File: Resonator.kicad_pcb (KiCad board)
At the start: 2 copper layers, 88 parts, among them J1 Conn_02x05_Odd_Even, U1 PCM3060, U2 R-78E5.0-0.5, U3 LD2981ABU33TR, U4 TL074, U5 STM32H750VBTx, U6 R-78E3.3-0.5

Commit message: Chanced regulators and oscillator work.
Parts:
- removed the C11 at (62.7, 30.0)
- removed the C13 at (44.7, 33.4)
- removed the C5 at (44.6, 27.6)
- removed the C7 at (48.4, 30.0)
- removed the L1 at (39.2, 30.9)
- removed the U2 at (53.1, 29.0)
- removed the U3 at (65.0, 34.8)
- added R2: 10k, Resistor_SMD:R_0603_1608Metric, B.Cu at (194.9, 90.2)
- added R3: 470, Resistor_SMD:R_0603_1608Metric, B.Cu at (158.0, 71.9)
- added SW1: SW_Push, Button_Switch_THT:SW_PUSH_6mm, B.Cu at (205.5, 86.5)
- added U4: LD2981ABU50TR, Package_TO_SOT_SMD:SOT-89-3, B.Cu at (184.5, 87.5)
- added Y1: ABM8G-25.000MHZ-18-D2Y-T, Crystal:Crystal_SMD_Abracon_ABM8G-4Pin_3.2x2.5mm, B.Cu at (163.3, 71.4)
- C1: renamed from C33; moved to B.Cu
- C10: renamed from C40; moved to B.Cu
- C11: renamed from C43; footprint Capacitor_SMD:C_0603_1608Metric -> Capacitor_SMD:C_0402_1005Metric; moved to B.Cu
- C12: renamed from C44; footprint Capacitor_SMD:C_0603_1608Metric -> Capacitor_SMD:C_0402_1005Metric; moved to B.Cu
- C13: renamed from C45; footprint Capacitor_SMD:C_0603_1608Metric -> Capacitor_SMD:C_0402_1005Metric; moved to B.Cu
- C14: renamed from C46; moved to B.Cu
- C15: renamed from C47; footprint Capacitor_SMD:C_0603_1608Metric -> Capacitor_SMD:C_0402_1005Metric; moved to B.Cu
- C16: renamed from C1; footprint Capacitor_SMD:C_0603_1608Metric -> Capacitor_SMD:C_0402_1005Metric; moved to B.Cu
- C17: renamed from C2; footprint Capacitor_SMD:C_0603_1608Metric -> Capacitor_SMD:C_0402_1005Metric; moved to B.Cu
- C18: renamed from C3; footprint Capacitor_SMD:C_0603_1608Metric -> Capacitor_SMD:C_0402_1005Metric; moved to B.Cu
- C19: renamed from C4; moved to B.Cu
- C2: renamed from C34; footprint Capacitor_SMD:C_0603_1608Metric -> Capacitor_SMD:C_0402_1005Metric; moved to B.Cu
- C20: renamed from C29; moved to B.Cu
- C21: renamed from C6; moved to B.Cu
- C22: renamed from C30; footprint Capacitor_SMD:C_0603_1608Metric -> Capacitor_SMD:C_0402_1005Metric; moved to B.Cu
- C23: renamed from C8; footprint Capacitor_SMD:C_0603_1608Metric -> Capacitor_SMD:C_0402_1005Metric; moved to B.Cu
- C24: renamed from C9; moved to B.Cu
- C25: renamed from C10; moved to B.Cu
- C26: renamed from C31; footprint Capacitor_SMD:C_0603_1608Metric -> Capacitor_SMD:C_0402_1005Metric; moved to B.Cu
- C27: renamed from C12; footprint Capacitor_SMD:C_0603_1608Metric -> Capacitor_SMD:C_0402_1005Metric; moved to B.Cu
- C28: renamed from C32; moved to B.Cu
- C29: renamed from C14; moved to B.Cu
- C3: renamed from C35; footprint Capacitor_SMD:C_0603_1608Metric -> Capacitor_SMD:C_0402_1005Metric; moved to B.Cu
- C30: renamed from C15; moved to B.Cu
- C31: renamed from C16; moved to B.Cu
- C32: renamed from C17; footprint Capacitor_SMD:C_0603_1608Metric -> Capacitor_SMD:C_0402_1005Metric; moved to B.Cu
- C33: renamed from C18; footprint Capacitor_SMD:C_0603_1608Metric -> Capacitor_SMD:C_0402_1005Metric; moved to B.Cu
- C34: renamed from C19; footprint Capacitor_SMD:C_0603_1608Metric -> Capacitor_SMD:C_0402_1005Metric; moved to B.Cu
- C35: renamed from C20; footprint Capacitor_SMD:C_0603_1608Metric -> Capacitor_SMD:C_0402_1005Metric; moved to B.Cu
- C36: renamed from C21; moved to B.Cu
- C37: renamed from C22; moved to B.Cu
- C38: renamed from C23; moved to B.Cu
- C39: renamed from C24; moved to B.Cu
- C4: renamed from C36; footprint Capacitor_SMD:C_0603_1608Metric -> Capacitor_SMD:C_0402_1005Metric; moved to B.Cu
- C40: renamed from C25; moved to B.Cu
- C41: renamed from C26; moved to B.Cu
- C42: renamed from C27; moved to B.Cu
- C43: renamed from C28; moved to B.Cu
- C5: renamed from C37; footprint Capacitor_SMD:C_0603_1608Metric -> Capacitor_SMD:C_0402_1005Metric; moved to B.Cu
- C6: renamed from C41; value 3p9 -> 22p; footprint Capacitor_SMD:C_0603_1608Metric -> Capacitor_SMD:C_0402_1005Metric; moved to B.Cu
- C7: renamed from C42; value 3p9 -> 22p; footprint Capacitor_SMD:C_0603_1608Metric -> Capacitor_SMD:C_0402_1005Metric; moved to B.Cu
- C8: renamed from C38; moved to B.Cu
- C9: renamed from C39; footprint Capacitor_SMD:C_0603_1608Metric -> Capacitor_SMD:C_0402_1005Metric; moved to B.Cu
- D1, D2, D3, D4, D5, D6, D7, FB1, FB2, J1: moved to B.Cu
- L1: renamed from L2; moved to B.Cu
- R1: renamed from R23; value 10k -> UNPOPULATED; moved to B.Cu
- R10: renamed from R7; moved to B.Cu
- R11: renamed from R8; moved to B.Cu
- R12: renamed from R9; moved to B.Cu
- R13: renamed from R10; moved to B.Cu
- R14: renamed from R11; moved to B.Cu
- R15: renamed from R12; moved to B.Cu
- R16: renamed from R13; moved to B.Cu
- R17: renamed from R14; moved to B.Cu
- R18: renamed from R15; moved to B.Cu
- R19: renamed from R16; moved to B.Cu
- R20: renamed from R17; moved to B.Cu
- R21: renamed from R18; moved to B.Cu
- R22: renamed from R19; moved to B.Cu
- R23: renamed from R20; moved to B.Cu
- R24: renamed from R21; moved to B.Cu
- R25: renamed from R22; moved to B.Cu
- R4: renamed from R1; moved to B.Cu
- R5: renamed from R2; moved to B.Cu
- R6: renamed from R3; moved to B.Cu
- R7: renamed from R4; moved to B.Cu
- R8: renamed from R5; moved to B.Cu
- R9: renamed from R6; moved to B.Cu
- U1: renamed from U5; moved to B.Cu
- U2: renamed from U1; moved to B.Cu
- U3: renamed from U6; moved to B.Cu
- U5: renamed from U4; moved to B.Cu
- moved J1 189.8 mm to (209.6, 74.3), turned to 0 degrees
- moved C30 182.6 mm to (205.9, 114.6), turned to 180 degrees
- moved D5 182.5 mm to (205.8, 110.8), turned to 180 degrees
- moved D7 182.5 mm to (205.8, 107.4), turned to 180 degrees
- moved U5 179.6 mm to (204.3, 102.5), turned to 180 degrees
- moved D2 178.2 mm to (203.6, 74.4), turned to 180 degrees
- moved D1 177.9 mm to (203.5, 64.1), turned to 0 degrees
- moved D3 177.9 mm to (203.5, 69.0), turned to 0 degrees
- moved C38 173.2 mm to (201.0, 115.4), turned to 180 degrees
- moved C32 173.0 mm to (200.9, 110.3), turned to 180 degrees
- moved C34 173.0 mm to (200.9, 112.8), turned to 180 degrees
- moved D4 171.3 mm to (200.1, 107.4), turned to 180 degrees
- moved R5 168.8 mm to (198.8, 69.0), turned to 180 degrees
- moved FB2 168.5 mm to (198.6, 64.3), turned to 0 degrees
- moved FB1 168.0 mm to (198.3, 74.4), turned to 0 degrees
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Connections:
- C21 pad 1: +5V -> +12V
- C23 pad 1: +5V -> +12V
- C27 pad 1: +3.3VA -> +5V
- C29 pad 1: +3.3VA -> +5V
- C7 pad 1: Net-(C42-Pad1) (its old number) -> Net-(C7-Pad1)
- R1 pad 2: Net-(R23-Pad2) -> +3V3
- U1 pad 13: Net-(C42-Pad1) (its old number) -> Net-(R3-Pad1)
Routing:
- net (no net): track 0.00 -> 18.3 mm
- net Net-(C6-Pad1): track 0.00 -> 8.58 mm
- net Net-(C7-Pad1): track 0.00 -> 3.93 mm

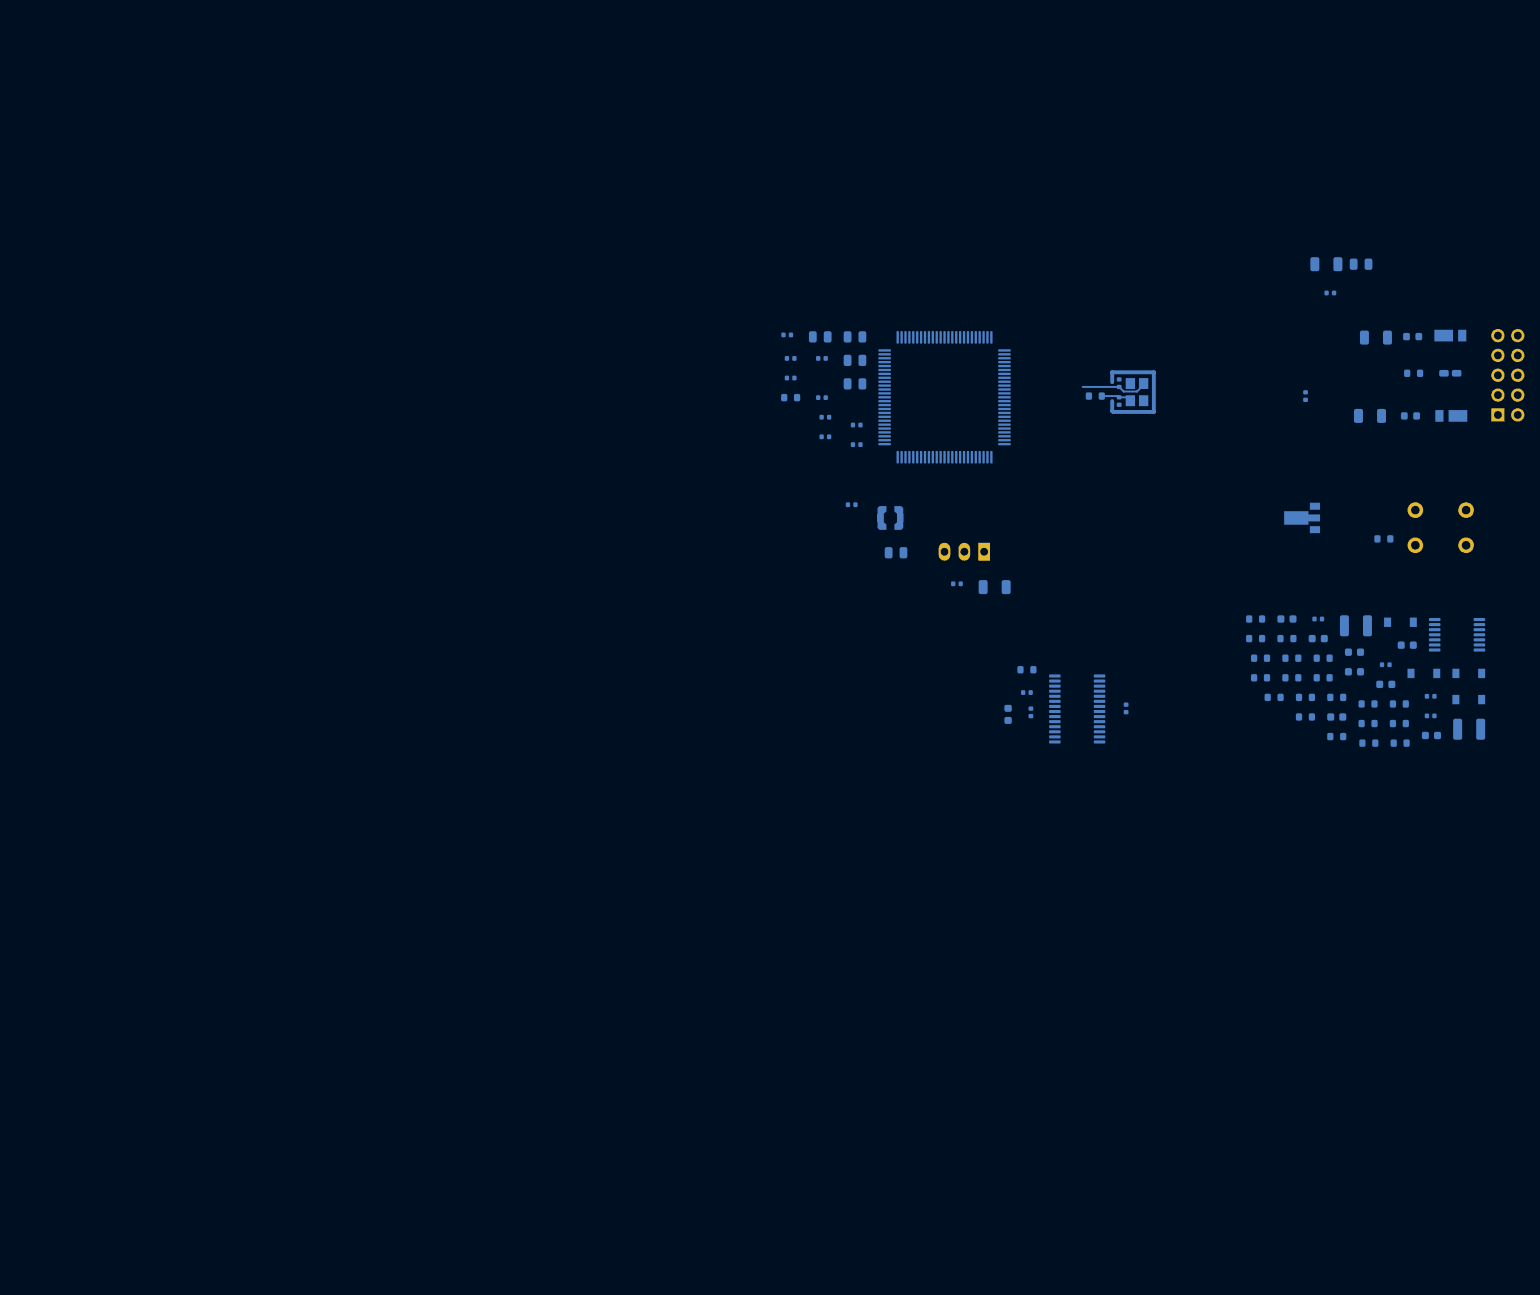
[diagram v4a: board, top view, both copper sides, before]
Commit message: Assigned pins and cleared schema rules.
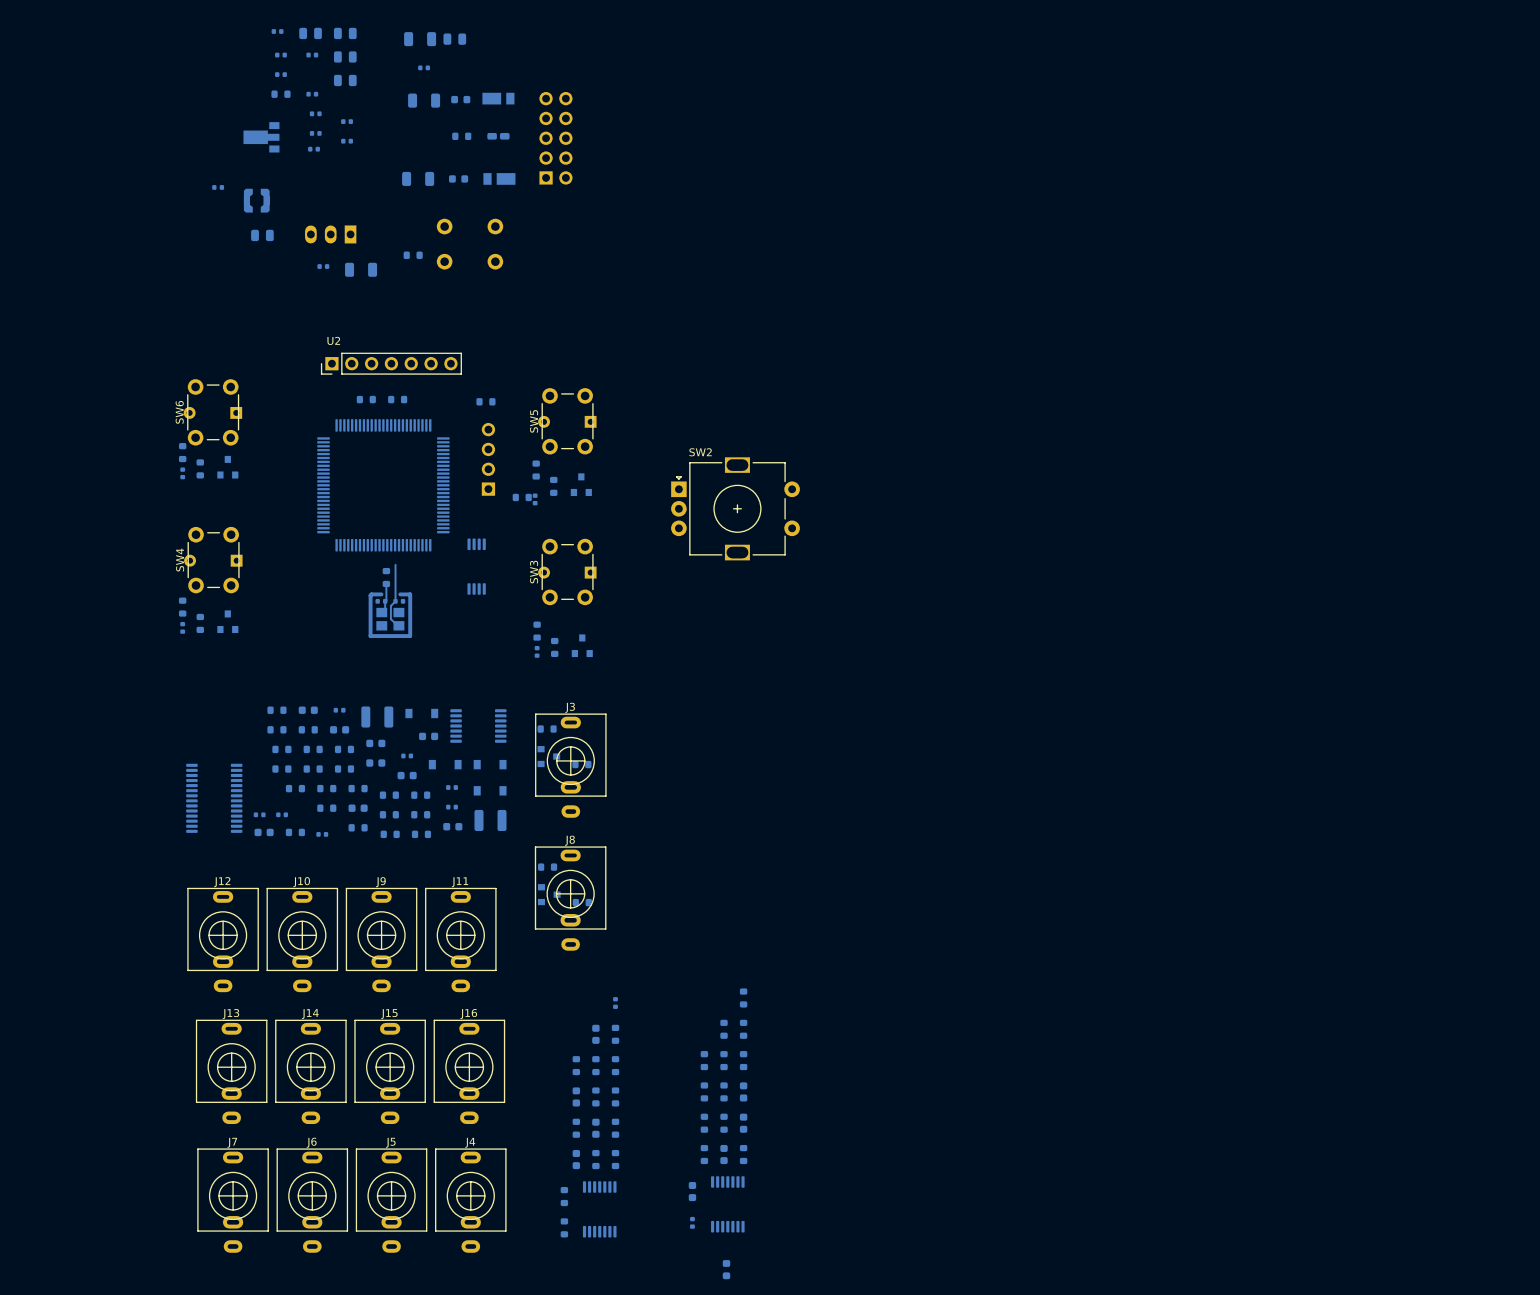
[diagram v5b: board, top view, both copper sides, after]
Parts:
- removed the C16 at (161.9, 111.9)
- removed the C17 at (149.2, 109.9)
- removed the C18 at (149.7, 112.4)
- removed the C19 at (146.8, 112.6)
- added C26: 100n, Capacitor_SMD:C_0402_1005Metric, B.Cu at (86.5, 104.6)
- added C27: 100n, Capacitor_SMD:C_0402_1005Metric, B.Cu at (106.4, 177.8)
- added C28: 470p, Capacitor_SMD:C_0603_1608Metric, B.Cu at (112.9, 165.0)
- added C29: 470p, Capacitor_SMD:C_0603_1608Metric, B.Cu at (106.4, 173.8)
- added C30: 470p, Capacitor_SMD:C_0603_1608Metric, B.Cu at (110.4, 169.0)
- added C31: 470p, Capacitor_SMD:C_0603_1608Metric, B.Cu at (112.9, 161.0)
- added C32: 100n, Capacitor_SMD:C_0402_1005Metric, B.Cu at (96.5, 149.6)
- added C33: 470p, Capacitor_SMD:C_0603_1608Metric, B.Cu at (94.0, 153.6)
- added C34: 470p, Capacitor_SMD:C_0603_1608Metric, B.Cu at (91.5, 161.7)
- added C35: 470p, Capacitor_SMD:C_0603_1608Metric, B.Cu at (91.5, 169.7)
- added C36: 470p, Capacitor_SMD:C_0603_1608Metric, B.Cu at (94.0, 165.7)
- added C37: 100n, Capacitor_SMD:C_0402_1005Metric, B.Cu at (41.1, 101.6)
- added C38: 100n, Capacitor_SMD:C_0402_1005Metric, B.Cu at (86.2, 85.1)
- added C39: 100n, Capacitor_SMD:C_0402_1005Metric, B.Cu at (41.1, 81.8)
- added C54: 100n, Capacitor_SMD:C_0402_1005Metric, B.Cu at (51.0, 125.5)
- added C55: 100n, Capacitor_SMD:C_0402_1005Metric, B.Cu at (53.8, 125.5)
- added C56: 10u, Capacitor_SMD:C_0603_1608Metric, B.Cu at (51.5, 127.8)
- added C57: 100n, Capacitor_SMD:C_0402_1005Metric, B.Cu at (59.0, 128.0)
- added FB3: Ferrite_Bead, Inductor_SMD:L_0603_1608Metric, B.Cu at (110.7, 183.8)
- added J1: Conn_01x04_Male, Connector_PinHeader_2.54mm:PinHeader_1x04_P2.54mm_Vertical, B.Cu at (80.3, 83.8)
- added J10: AudioJack2_SwitchT, Local:PJ398SM, F.Cu at (56.4, 140.9)
- added J11: AudioJack2_SwitchT, Local:PJ398SM, F.Cu at (76.7, 140.9)
- added J12: AudioJack2_SwitchT, Local:PJ398SM, F.Cu at (46.3, 140.9)
- added J13: AudioJack2_SwitchT, Local:PJ398SM, F.Cu at (47.4, 157.8)
- added J14: AudioJack2_SwitchT, Local:PJ398SM, F.Cu at (57.5, 157.8)
- added J15: AudioJack2_SwitchT, Local:PJ398SM, F.Cu at (67.7, 157.8)
- added J16: AudioJack2_SwitchT, Local:PJ398SM, F.Cu at (77.8, 157.8)
- added J3: AudioJack2_SwitchT, Local:PJ398SM, F.Cu at (90.8, 118.6)
- added J4: AudioJack2_SwitchT, Local:PJ398SM, F.Cu at (78.0, 174.3)
- added J5: AudioJack2_SwitchT, Local:PJ398SM, F.Cu at (67.8, 174.3)
- added J6: AudioJack2_SwitchT, Local:PJ398SM, F.Cu at (57.7, 174.3)
- added J7: AudioJack2_SwitchT, Local:PJ398SM, F.Cu at (47.5, 174.3)
- added J8: AudioJack2_SwitchT, Local:PJ398SM, F.Cu at (90.8, 135.6)
- added J9: AudioJack2_SwitchT, Local:PJ398SM, F.Cu at (66.6, 140.9)
- added Q1: BC847, Package_TO_SOT_SMD:SOT-23, B.Cu at (92.3, 103.9)
- added Q2: BC847, Package_TO_SOT_SMD:SOT-23, B.Cu at (88.0, 118.1)
- added Q3: BC847, Package_TO_SOT_SMD:SOT-23, B.Cu at (88.0, 135.7)
- added Q4: BC847, Package_TO_SOT_SMD:SOT-23, B.Cu at (46.9, 100.8)
- added Q5: BC847, Package_TO_SOT_SMD:SOT-23, B.Cu at (92.2, 83.2)
- added Q6: BC847, Package_TO_SOT_SMD:SOT-23, B.Cu at (46.9, 81.0)
- added R10: 10k, Resistor_SMD:R_0603_1608Metric, B.Cu at (86.5, 102.0)
- added R11: 100k, Resistor_SMD:R_0603_1608Metric, B.Cu at (87.8, 114.5)
- added R12: 10k, Resistor_SMD:R_0603_1608Metric, B.Cu at (92.2, 119.1)
- added R13: 169k, Resistor_SMD:R_0603_1608Metric, B.Cu at (110.4, 157.0)
- added R14: 100k, Resistor_SMD:R_0603_1608Metric, B.Cu at (107.9, 161.0)
- added R15: 200k, Resistor_SMD:R_0603_1608Metric, B.Cu at (107.9, 157.0)
- added R16: 100k, Resistor_SMD:R_0603_1608Metric, B.Cu at (110.4, 153.0)
- added R17: 33k, Resistor_SMD:R_0603_1608Metric, B.Cu at (112.9, 149.0)
- added R18: 56k, Resistor_SMD:R_0603_1608Metric, B.Cu at (112.9, 153.0)
- added R19: 200k, Resistor_SMD:R_0603_1608Metric, B.Cu at (112.9, 157.0)
- added R20: 100k, Resistor_SMD:R_0603_1608Metric, B.Cu at (110.4, 161.0)
- added R21: 200k, Resistor_SMD:R_0603_1608Metric, B.Cu at (107.9, 165.0)
- added R22: 100k, Resistor_SMD:R_0603_1608Metric, B.Cu at (107.9, 169.0)
- added R23: 56k, Resistor_SMD:R_0603_1608Metric, B.Cu at (112.9, 169.0)
- added R24: 56k, Resistor_SMD:R_0603_1608Metric, B.Cu at (110.4, 165.0)
- added R25: 100k, Resistor_SMD:R_0603_1608Metric, B.Cu at (87.8, 132.2)
- added R26: 10k, Resistor_SMD:R_0603_1608Metric, B.Cu at (92.3, 136.8)
- added R27: 169k, Resistor_SMD:R_0603_1608Metric, B.Cu at (96.5, 161.7)
- added R28: 100k, Resistor_SMD:R_0603_1608Metric, B.Cu at (96.5, 165.7)
- added R29: 200k, Resistor_SMD:R_0603_1608Metric, B.Cu at (96.5, 169.7)
- added R30: 100k, Resistor_SMD:R_0603_1608Metric, B.Cu at (90.0, 174.4)
- added R31: 33k, Resistor_SMD:R_0603_1608Metric, B.Cu at (91.5, 165.7)
- added R32: 56k, Resistor_SMD:R_0603_1608Metric, B.Cu at (94.0, 169.7)
- added R33: 200k, Resistor_SMD:R_0603_1608Metric, B.Cu at (94.0, 161.7)
- added R34: 100k, Resistor_SMD:R_0603_1608Metric, B.Cu at (96.5, 157.6)
- added R35: 200k, Resistor_SMD:R_0603_1608Metric, B.Cu at (96.5, 153.6)
- added R36: 100k, Resistor_SMD:R_0603_1608Metric, B.Cu at (94.0, 157.6)
- added R37: 56k, Resistor_SMD:R_0603_1608Metric, B.Cu at (90.0, 178.4)
- added R38: 56k, Resistor_SMD:R_0603_1608Metric, B.Cu at (91.5, 157.6)
- added R39: 47, Resistor_SMD:R_0603_1608Metric, B.Cu at (43.3, 101.0)
- added R40: 10k, Resistor_SMD:R_0603_1608Metric, B.Cu at (41.1, 98.9)
- added R41: 47, Resistor_SMD:R_0603_1608Metric, B.Cu at (88.6, 83.4)
- added R42: 10k, Resistor_SMD:R_0603_1608Metric, B.Cu at (86.4, 81.4)
- added R43: 47, Resistor_SMD:R_0603_1608Metric, B.Cu at (43.3, 81.2)
- added R44: 10k, Resistor_SMD:R_0603_1608Metric, B.Cu at (41.1, 79.1)
- added R5: 1k, Resistor_SMD:R_0603_1608Metric, B.Cu at (84.6, 84.9)
- added R6: 10k, Resistor_SMD:R_0603_1608Metric, B.Cu at (79.9, 72.6)
- added R65: 220k, Resistor_SMD:R_0603_1608Metric, B.Cu at (55.5, 127.8)
- added R7: 10k, Resistor_SMD:R_0603_1608Metric, B.Cu at (68.6, 72.3)
- added R9: 47, Resistor_SMD:R_0603_1608Metric, B.Cu at (88.7, 104.1)
- added SW2: Rotary_Encoder_Switch, Rotary_Encoder:RotaryEncoder_Alps_EC11E-Switch_Vertical_H20mm, F.Cu at (104.6, 83.8)
- added SW3: SW_Push_LED, Local:SW_PUSH_LED_6mm, F.Cu at (90.4, 94.5)
- added SW4: SW_Push_LED, Local:SW_PUSH_LED_6mm, F.Cu at (45.1, 93.0)
- added SW5: SW_Push_LED, Local:SW_PUSH_LED_6mm, F.Cu at (90.4, 75.2)
- added SW6: SW_Push_LED, Local:SW_PUSH_LED_6mm, F.Cu at (45.0, 74.0)
- added U3: AT25xxx, Package_SO:TSSOP-8_4.4x3mm_P0.65mm, B.Cu at (78.7, 93.7)
- added U6: MCP6004, Package_SO:TSSOP-14_4.4x5mm_P0.65mm, B.Cu at (110.9, 175.4)
- added U7: MCP6004, Package_SO:TSSOP-14_4.4x5mm_P0.65mm, B.Cu at (94.5, 176.1)
- added U9: PCM3060, Package_SO:TSSOP-28_4.4x9.7mm_P0.65mm, B.Cu at (45.1, 123.4)
- R4: value 220k -> 10k
- U2: value PCM3060 -> IPS240x240; footprint Package_SO:TSSOP-28_4.4x9.7mm_P0.65mm -> Local:IPS240x240; moved to F.Cu
- moved U5 141.9 mm to (51.2, 38.7)
- moved C19 130.9 mm to (57.9, 40.3), turned to 180 degrees
- moved R2 129.5 mm to (70.6, 53.8)
- moved SW1 129.5 mm to (81.1, 50.2)
- moved C41 125.9 mm to (72.6, 115.5)
- moved C42 125.9 mm to (63.6, 124.7)
- moved C48 125.9 mm to (75.6, 122.0)
- moved C49 125.9 mm to (69.8, 118.0)
- moved C50 125.9 mm to (69.8, 120.5)
- moved C52 125.9 mm to (75.6, 124.5)
- moved R47 125.9 mm to (63.6, 122.2)
- moved R48 125.9 mm to (57.8, 117.1)
- moved R52 125.9 mm to (57.8, 119.6)
- moved R55 125.9 mm to (63.6, 127.2)
- moved C40 125.9 mm to (75.7, 127.0)
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- renumbered C20 to C16, C21 to C17, C22 to C18, C23 to C19, C24 to C20, C25 to C21, C26 to C22, C27 to C23, C28 to C24, C29 to C25, C38 to C40, C39 to C41, C40 to C42, C41 to C43, C30 to C44, C31 to C45, C42 to C46, C43 to C47, C32 to C48, C33 to C49, C36 to C50, C37 to C51, C34 to C52, C35 to C53, J1 to J2, R12 to R45, R13 to R46, R14 to R47, R15 to R48, R16 to R49, R17 to R50, R18 to R51, R19 to R52, R20 to R53, R21 to R54, R22 to R55, R23 to R56, R6 to R57, R7 to R58, R24 to R59, R25 to R60, R8 to R61, R9 to R62, R10 to R63, R11 to R64, R5 to R8, U3 to U4, U4 to U5, U5 to U8
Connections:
- net Net-(C12-Pad1) renamed RESET
- C44 pad 2: InL -> Net-(C44-Pad2)
- C45 pad 2: InR -> Net-(C45-Pad2)
- C8 pad 1: Net-(C10-Pad1) -> Net-(C8-Pad1)
- R4 pad 1: GND -> +3V3
- R4 pad 2: Net-(R4-Pad2) -> TIM3_CH2
- R59 pad 1: OutR -> Net-(J16-PadT)
- R60 pad 1: OutL -> Net-(J15-PadT)
- U1 pad 15: Net-(U1-Pad15) -> PC0
- U1 pad 16: Net-(U1-Pad16) -> PC1
- U1 pad 17: Net-(U1-Pad17) -> PC2
- U1 pad 18: Net-(U1-Pad18) -> PC3
- U1 pad 20: Net-(U1-Pad20) -> +3.3VA
- U1 pad 22: Net-(U1-Pad22) -> PA0
- U1 pad 23: Net-(U1-Pad23) -> PA1
- U1 pad 24: Net-(U1-Pad24) -> PA2
- U1 pad 25: Net-(U1-Pad25) -> PA3
- U1 pad 28: Net-(U1-Pad28) -> I2S1_WS
- U1 pad 29: Net-(U1-Pad29) -> I2S1_CK
- U1 pad 30: Net-(U1-Pad30) -> I2S1_SDI
- U1 pad 31: Net-(U1-Pad31) -> I2S1_SDO
- U1 pad 32: Net-(U1-Pad32) -> I2S1_MCK
- U1 pad 33: Net-(U1-Pad33) -> PC5
- U1 pad 34: Net-(U1-Pad34) -> PB0
- U1 pad 35: Net-(U1-Pad35) -> PB1
- U1 pad 48: Net-(C10-Pad1) -> Net-(C8-Pad1)
- U1 pad 51: Net-(U1-Pad51) -> PB12
- U1 pad 52: Net-(U1-Pad52) -> SPI2_SCK
- U1 pad 53: Net-(U1-Pad53) -> PB14
- U1 pad 54: Net-(U1-Pad54) -> SPI2_MOSI
- U1 pad 56: Net-(U1-Pad56) -> PD9
- U1 pad 57: Net-(U1-Pad57) -> PD10
- U1 pad 58: Net-(U1-Pad58) -> PD11
- U1 pad 59: Net-(U1-Pad59) -> PD12
- U1 pad 60: Net-(U1-Pad60) -> PD13
- U1 pad 61: Net-(U1-Pad61) -> PD14
- U1 pad 63: Net-(U1-Pad63) -> TIM3_CH1
- U1 pad 64: Net-(U1-Pad64) -> TIM3_CH2
- U1 pad 65: Net-(U1-Pad65) -> PC8
- U1 pad 72: Net-(U1-Pad72) -> SWDIO
- U1 pad 76: Net-(U1-Pad76) -> SWCLK
- U1 pad 81: Net-(U1-Pad81) -> PD0
- U1 pad 82: Net-(U1-Pad82) -> PD1
- U1 pad 83: Net-(U1-Pad83) -> PD2
- U1 pad 84: Net-(U1-Pad84) -> PD3
- U1 pad 89: Net-(U1-Pad89) -> SPI3_SCK
- U1 pad 90: Net-(U1-Pad90) -> SPI3_MISO
- U1 pad 91: Net-(U1-Pad91) -> SPI3_MOSI
- U1 pad 92: Net-(U1-Pad92) -> PB6
- U2 pad 2: GND -> +3V3
- U2 pad 3: PA11 -> SPI2_SCK
- U2 pad 4: PF0 -> Net-(R5-Pad1)
- U2 pad 5: PF1 -> PB12
- U2 pad 6: PA8 -> PB14
